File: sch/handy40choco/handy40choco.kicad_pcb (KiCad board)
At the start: 2 copper layers, 175 x 112 mm, 147 parts, among them J1 Conn_01x02, J2 Conn_02x08_Odd_Even, J3 USB_C_Receptacle_USB2.0_16P, J4 Conn_01x04, Q1 DMG2301L, SW1 SW_Push, SW10 SW_Push, SW11 SW_Push, SW12 SW_Push, SW13 SW_Push, SW14 SW_Push, SW15 SW_Push, SW16 SW_Push, SW17 SW_Push, SW18 SW_Push, SW19 SW_Push, SW2 SW_Push, SW20 SW_Push, SW21 SW_Push, SW22 SW_Push, SW23 SW_Push, SW24 SW_Push, SW25 SW_Push, SW26 SW_Push, SW27 SW_Push, SW28 SW_Push, SW29 SW_Push, SW3 SW_Push, SW30 SW_Push, SW31 SW_Push, SW32 SW_Push, SW33 SW_Push, SW34 SW_Push, SW35 SW_Push, SW36 SW_Push, SW37 SW_Push, SW38 SW_Push, SW39 SW_Push, SW4 SW_Push, SW40 SW_Push, SW41 SW_Push, SW42 SW_Push, SW5 SW_Push, SW6 SW_Push, SW7 SW_Push, SW8 SW_Push, SW9 SW_Push, U1 Pico, U2 pimoroni lcd, U3 ESP32-S3-WROOM-1, U4 MIC5219-3.3YM5, Y1 32k

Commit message: Kicad 9に変更しました。 マイコン基板から16ピンのピンヘッダに変更しました。
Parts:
- removed C1: 10u, Capacitor_SMD:C_0603_1608Metric_Pad1.08x0.95mm_HandSolder
- removed C2, C3: 100n, Capacitor_SMD:C_0603_1608Metric_Pad1.08x0.95mm_HandSolder
- removed C4: 1u, Capacitor_SMD:C_0603_1608Metric_Pad1.08x0.95mm_HandSolder
- removed C5: 470p, Capacitor_SMD:C_0603_1608Metric_Pad1.08x0.95mm_HandSolder
- removed C6: 10n, Capacitor_SMD:C_0603_1608Metric_Pad1.08x0.95mm_HandSolder
- removed C7, C8: 15p, Capacitor_SMD:C_0603_1608Metric_Pad1.08x0.95mm_HandSolder
- removed D41, D42, D43: D_Schottky, Diode_SMD:D_SOD-123
- removed D44, D45, D46: D_TVS, Diode_SMD:D_SOD-123
- removed D47, D48, D49, D50, D51, D52, D53: LED, LED_SMD:LED_0603_1608Metric_Pad1.05x0.95mm_HandSolder
- removed F1: Polyfuse_Small, Fuse:Fuse_Littelfuse-NANO2-451_453
- removed J2: Conn_02x08_Odd_Even, my_pico:oled_PinSocket_2x08_P2.54mm_Vertical
- removed J3: USB_C_Receptacle_USB2.0_16P, Connector_USB:USB_C_Receptacle_XKB_U262-16XN-4BVC11
- removed J4: Conn_01x04, Connector_JST:JST_XH_B4B-XH-A_1x04_P2.50mm_Vertical
- removed Q1: DMG2301L, Package_TO_SOT_SMD:SOT-23
- removed R1, R11, R12, R2, R8, R9: 0, Resistor_SMD:R_0603_1608Metric
- removed R10: [10M], Resistor_SMD:R_0603_1608Metric
- removed R13, R14, R15, R16, R17, R18, R19: 1k, Resistor_SMD:R_0603_1608Metric
- removed R3, R4, R7: 10k, Resistor_SMD:R_0603_1608Metric
- removed R5, R6: 5.1k, Resistor_SMD:R_0603_1608Metric
- removed SW41, SW42: SW_Push, Button_Switch_SMD:SW_Push_SPST_NO_Alps_SKRK
- removed U1: Pico, my_pico:pico_no_dbg_smd_th_p0.85
- removed U2: pimoroni lcd, my_pico:pimoroni_lcd_p0.85
- removed U3: ESP32-S3-WROOM-1, RF_Module:ESP32-S3-WROOM-1
- removed U4: MIC5219-3.3YM5, Package_TO_SOT_SMD:SOT-23-5
- removed Y1: 32k, Crystal:Crystal_SMD_2012-2Pin_2.0x1.2mm_HandSoldering
- J1: value Conn_01x02 -> Conn_01x20; footprint Connector_JST:JST_PH_B2B-PH-K_1x02_P2.00mm_Vertical -> Connector_PinHeader_2.54mm:PinHeader_1x20_P2.54mm_Vertical
- moved J1 35.9 mm to (210.0, 87.0), turned to -90 degrees
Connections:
- J1 pad 1: /VBAT -> /ROW3
- J1 pad 2: GND -> /ROW2
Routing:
- net +3.3V: track 170.8 -> 0.00 mm, vias 3 -> 0
- net /COL0: track 216.7 -> 61.8 mm
- net /COL1: track 206.4 -> 65.9 mm
- net /COL2: track 186.6 -> 57.9 mm
- net /COL3: track 173.0 -> 60.4 mm
- net /LCD_RESET: track 111.5 -> 0.00 mm
- net /COL4: track 155.4 -> 58.4 mm
- net /LCD_TE: track 92.0 -> 0.00 mm
- net /LCD_BL: track 86.7 -> 0.00 mm
- net /ROW3: track 291.0 -> 204.5 mm
- net /COL5: track 142.1 -> 60.4 mm
- net /COL6: track 132.1 -> 57.9 mm
- net /OLED_RESET: track 71.9 -> 0.00 mm
- net /ROW2: track 274.4 -> 205.2 mm
- net /DATA: track 61.2 -> 0.00 mm
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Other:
- board size 175 x 112 mm -> 175 x 72.5 mm

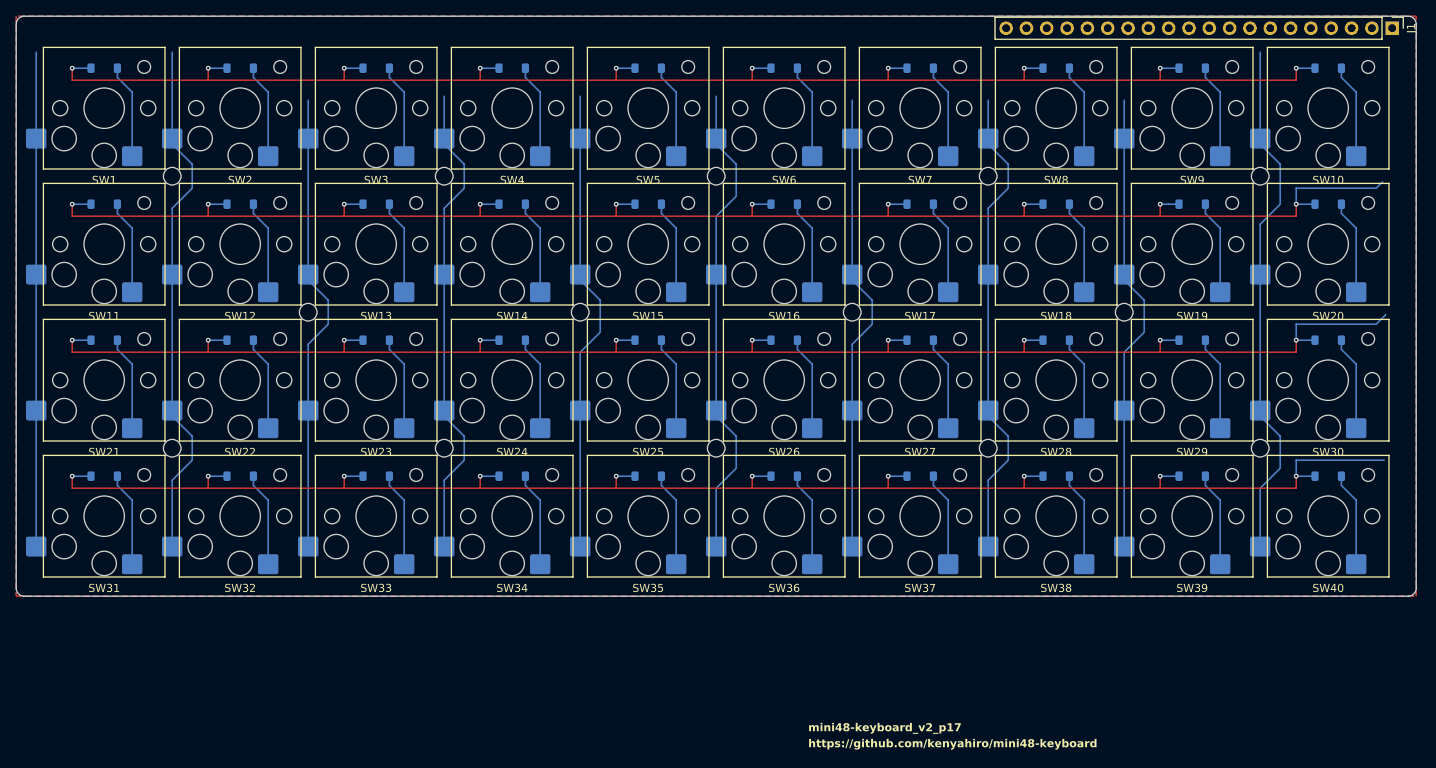
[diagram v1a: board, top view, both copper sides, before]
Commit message: 配線を完了しました。 シルクの位置を調整しました。
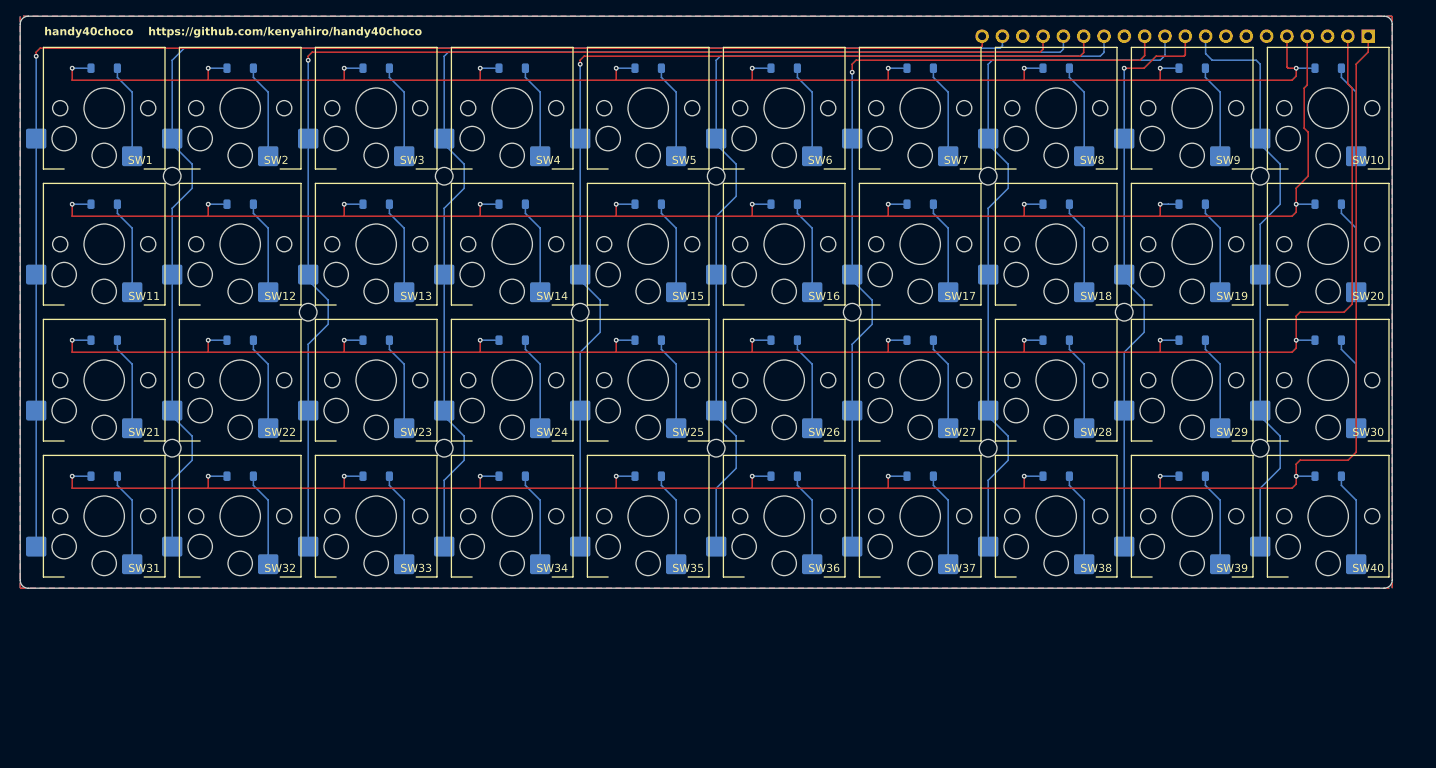
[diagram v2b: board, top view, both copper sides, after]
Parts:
- J1: moved to B.Cu
- SW1, SW10, SW11, SW12, SW13, SW14, SW15, SW16, SW17, SW18, SW19, SW2, SW20, SW21, SW22, SW23, SW24, SW25, SW26, SW27, SW28, SW29, SW3, SW30, SW31, SW32, SW33, SW34, SW35, SW36, SW37, SW38, SW39, SW4, SW40, SW5, SW6, SW7, SW8, SW9: footprint my_keyswitch:SW_Hotswap_Kailh_Choc_V1V2 -> my_keyswitch:SW_Hotswap_Kailh_Choc_V1V2_no_mp
- moved J1 3.16 mm to (207.0, 88.0), turned to 90 degrees
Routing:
- net /COL0: track 61.8 -> 181.6 mm, vias 0 -> 1
- net /COL1: track 65.9 -> 170.7 mm
- net /COL2: track 57.9 -> 157.2 mm, vias 0 -> 1
- net /COL3: track 60.4 -> 144.8 mm
- net /COL4: track 58.4 -> 128.3 mm, vias 0 -> 1
- net /COL5: track 60.4 -> 115.8 mm
- net /ROW3: track 204.5 -> 253.4 mm
- net /COL6: track 57.9 -> 101.8 mm, vias 0 -> 1
- net /ROW2: track 205.2 -> 235.6 mm
- net /COL7: track 59.9 -> 89.4 mm
- net /COL8: track 57.9 -> 72.6 mm, vias 0 -> 1
- net /ROW1: track 204.6 -> 213.2 mm
- net /COL9: track 65.9 -> 74.0 mm
- net /ROW0: track 191.5 -> 196.3 mm
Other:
- board size 175 x 72.5 mm -> 171.5 x 71.5 mm
- board text added: "handy40choco"
- board text added: "https://github.com/kenyahiro/handy40choco"
- board text removed: "https://github.com/kenyahiro/mini48-keyboard"
- board text removed: "mini48-keyboard_v2_p17"

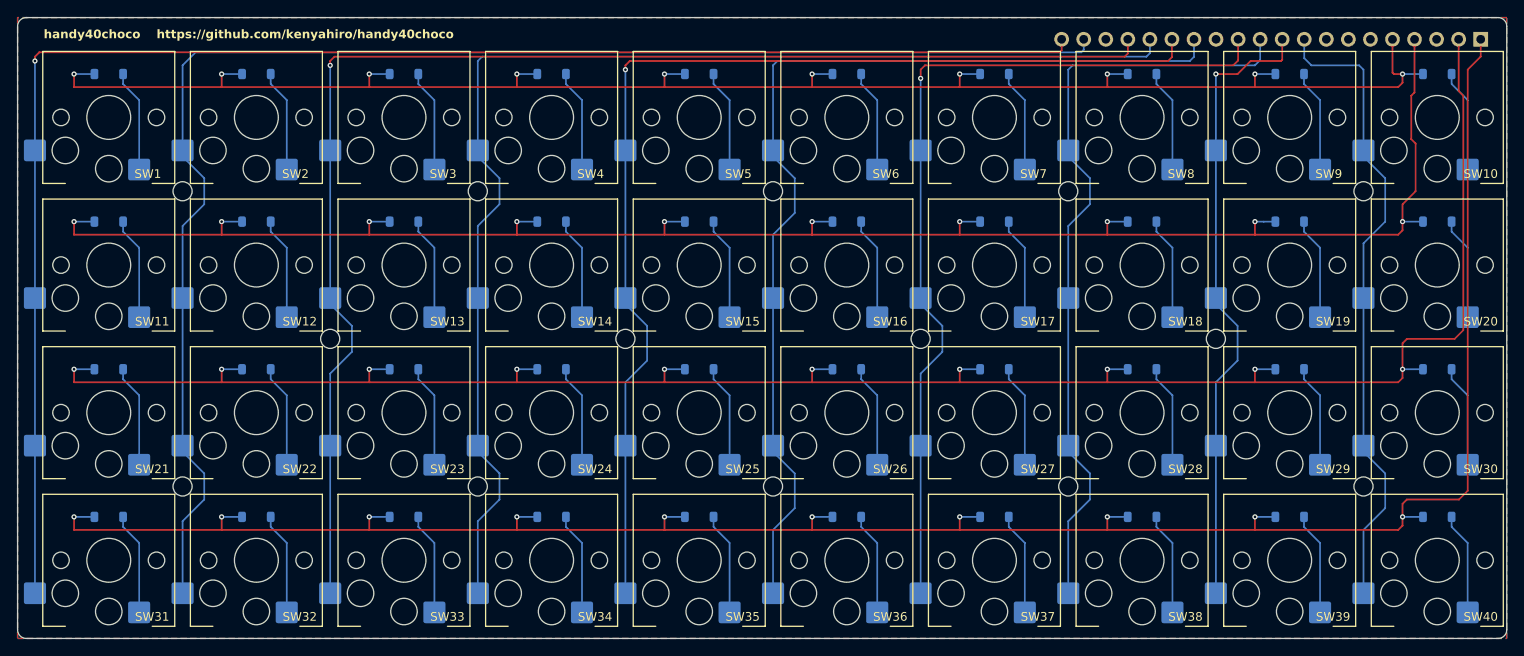
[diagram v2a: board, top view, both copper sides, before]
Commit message: 電気図面のpdfを追加しました。 PCBのFABにピンヘッダの寸法線を追記しました。
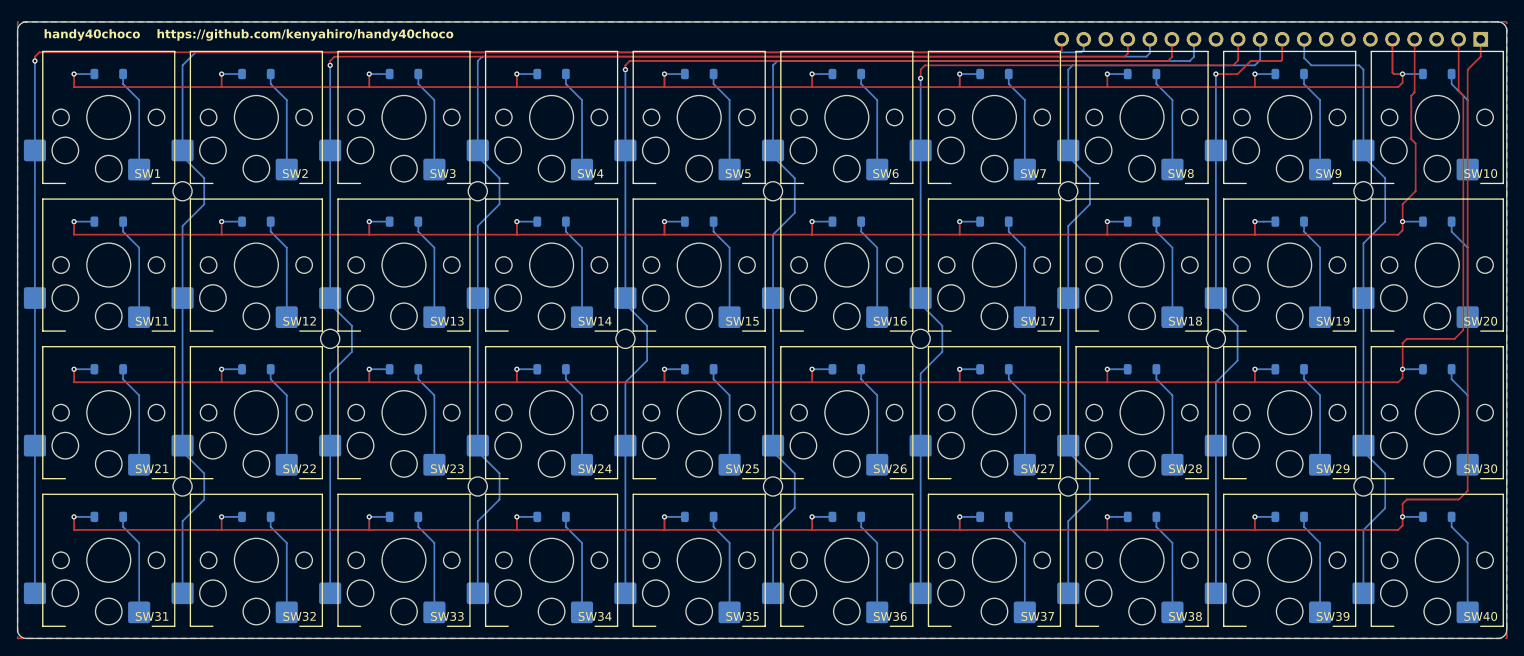
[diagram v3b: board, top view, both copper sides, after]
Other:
- board size 171.5 x 71.5 mm -> 171.5 x 71 mm
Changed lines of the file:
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@@
 		(allow_soldermask_bridges_in_footprints no)
 		(tenting front back)
-		(aux_axis_origin 38.5 85.5)
-		(grid_origin 38.5 85.5)
+		(aux_axis_origin 38.5 86)
+		(grid_origin 38.5 86)
 		(pcbplotparams
-			(layerselection 0x00000000_00000000_55555555_5755f5ff)
-			(plot_on_all_layers_selection 0x00000000_00000000_00000000_00000000)
+			(layerselection 0x00000000_00000000_5555555d_5755f5ff)
+			(plot_on_all_layers_selection 0x00000000_00000000_00000008_00000000)
 			(disableapertmacros no)
 			(usegerberextensions yes)
@@
 			(dashed_line_gap_ratio 3.000000)
 			(svgprecision 4)
-			(plotframeref no)
+			(plotframeref yes)
 			(mode 1)
 			(useauxorigin no)
@@
 			(pdf_back_fp_property_popups yes)
 			(pdf_metadata yes)
-			(pdf_single_document no)
+			(pdf_single_document yes)
 			(dxfpolygonmode yes)
 			(dxfimperialunits yes)
@@
 			(psnegative no)
 			(psa4output no)
-			(plot_black_and_white yes)
+			(plot_black_and_white no)
 			(sketchpadsonfab no)
 			(plotpadnumbers no)
@@
 			(crossoutdnponfab yes)
 			(subtractmaskfromsilk yes)
-			(outputformat 1)
+			(outputformat 4)
 			(mirror no)
-			(drillshape 0)
+			(drillshape 2)
 			(scaleselection 1)
 			(outputdirectory "gerber")
@@
 	)
 	(gr_arc
-		(start 209 85.5)
-		(mid 209.707107 85.792893)
-		(end 210 86.5)
+		(start 209 86)
+		(mid 209.707107 86.292893)
+		(end 210 87)
 		(stroke
 			(width 0.05)
@@
 	)
 	(gr_line
-		(start 210 86.5)
+		(start 210 87)
 		(end 210 156)
 		(stroke
@@
 	)
 	(gr_line
-		(start 39.5 85.5)
-		(end 209 85.5)
+		(start 39.5 86)
+		(end 209 86)
 		(stroke
 			(width 0.05)
@@
 	(gr_line
 		(start 38.5 156)
-		(end 38.5 86.5)
+		(end 38.5 87)
 		(stroke
 			(width 0.05)
@@
 	)
 	(gr_arc
-		(start 38.5 86.5)
-		(mid 38.792893 85.792893)
-		(end 39.5 85.5)
+		(start 38.5 87)
+		(mid 38.792893 86.292893)
+		(end 39.5 86)
 		(stroke
 			(width 0.05)
@@
 		(layer "F.Fab")
 		(pts
-			(xy 210 85.5) (xy 210 157)
+			(xy 209 86) (xy 209 157)
 		)
-		(height 53)
+		(height 55.5)
 		(orientation 1)
 		(format
@@
 			(keep_text_aligned yes)
 		)
-		(gr_text "71.5000 mm"
-			(at 261.85 121.25 90)
+		(gr_text "71.0000 mm"
+			(at 263.35 121.5 90)
+			(layer "F.Fab")
+			(effects
+				(font
+					(size 1 1)
+					(thickness 0.15)
+				)
+			)
+		)
+	)
+	(dimension
+		(type orthogonal)
+		(layer "F.Fab")
+		(pts
+			(xy 207 88) (xy 210 88)
+		)
+		(height -15.5)
+		(orientation 0)
+		(format
+			(prefix "")
+			(suffix "")
+			(units 3)
+			(units_format 1)
+			(precision 4)
+		)
+		(style
+			(thickness 0.1)
+			(arrow_length 1.27)
+			(text_position_mode 0)
+			(arrow_direction outward)
+			(extension_height 0.58642)
+			(extension_offset 0.5)
+			(keep_text_aligned yes)
+		)
+		(gr_text "3.0000 mm"
+			(at 208.5 71.35 0)
+			(layer "F.Fab")
+			(effects
+				(font
+					(size 1 1)
+					(thickness 0.15)
+				)
+			)
+		)
+	)
+	(dimension
+		(type orthogonal)
+		(layer "F.Fab")
+		(pts
+			(xy 207 88) (xy 207 86)
+		)
+		(height 17)
+		(orientation 1)
+		(format
+			(prefix "")
+			(suffix "")
+			(units 3)
+			(units_format 1)
+			(precision 4)
+		)
+		(style
+			(thickness 0.1)
+			(arrow_length 1.27)
+			(text_position_mode 0)
+			(arrow_direction outward)
+			(extension_height 0.58642)
+			(extension_offset 0.5)
+			(keep_text_aligned yes)
+		)
+		(gr_text "2.0000 mm"
+			(at 222.85 87 90)
 			(layer "F.Fab")
 			(effects
@@
 		(polygon
 			(pts
-				(xy 38.5 85.5) (xy 38.5 157) (xy 210 157) (xy 210 85.5)
+				(xy 38.5 86) (xy 38.5 157) (xy 210 157) (xy 210 86)
 			)
 		)
@@
 		(polygon
 			(pts
-				(xy 38.5 85.5) (xy 38.5 157) (xy 210 157) (xy 210 85.5)
+				(xy 38.5 86) (xy 38.5 157) (xy 210 157) (xy 210 86)
 			)
 		)

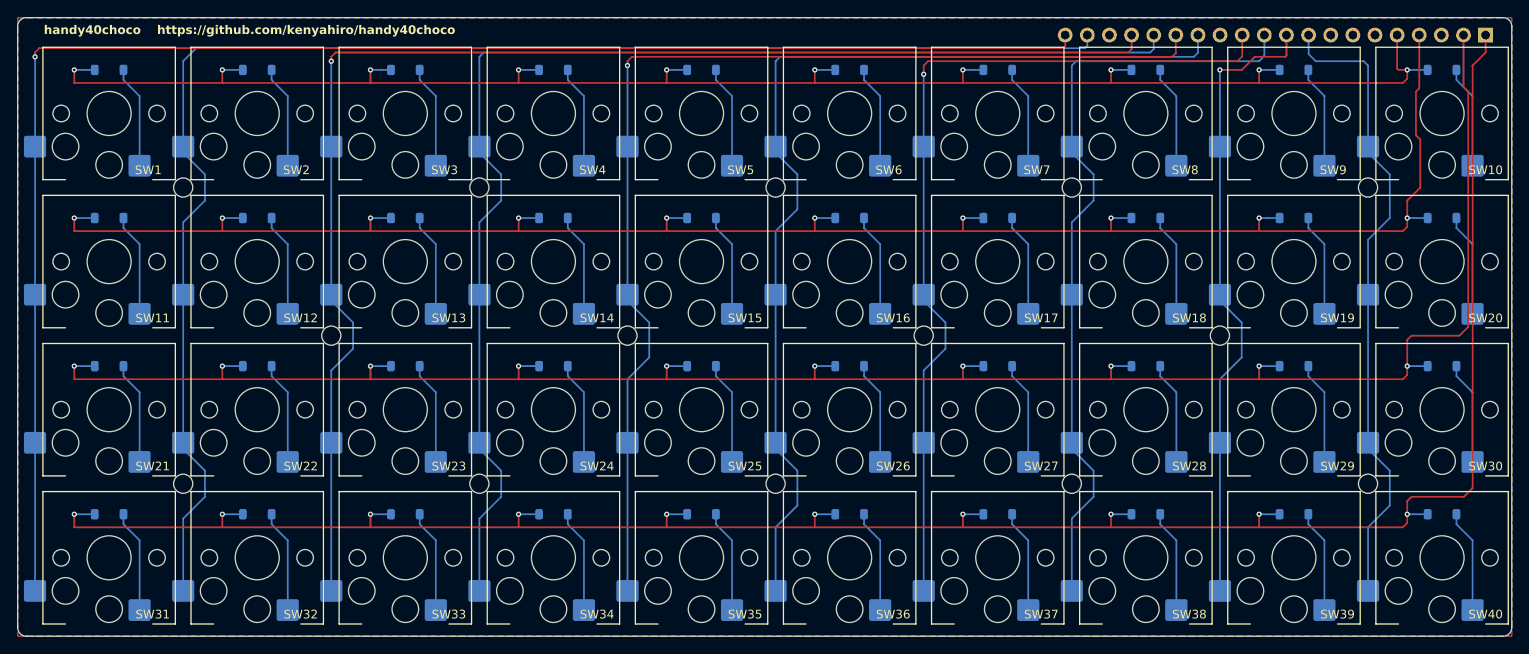
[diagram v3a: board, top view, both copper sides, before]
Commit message: 左端のキーの向きを180度回転させて、基板幅を短くしました。
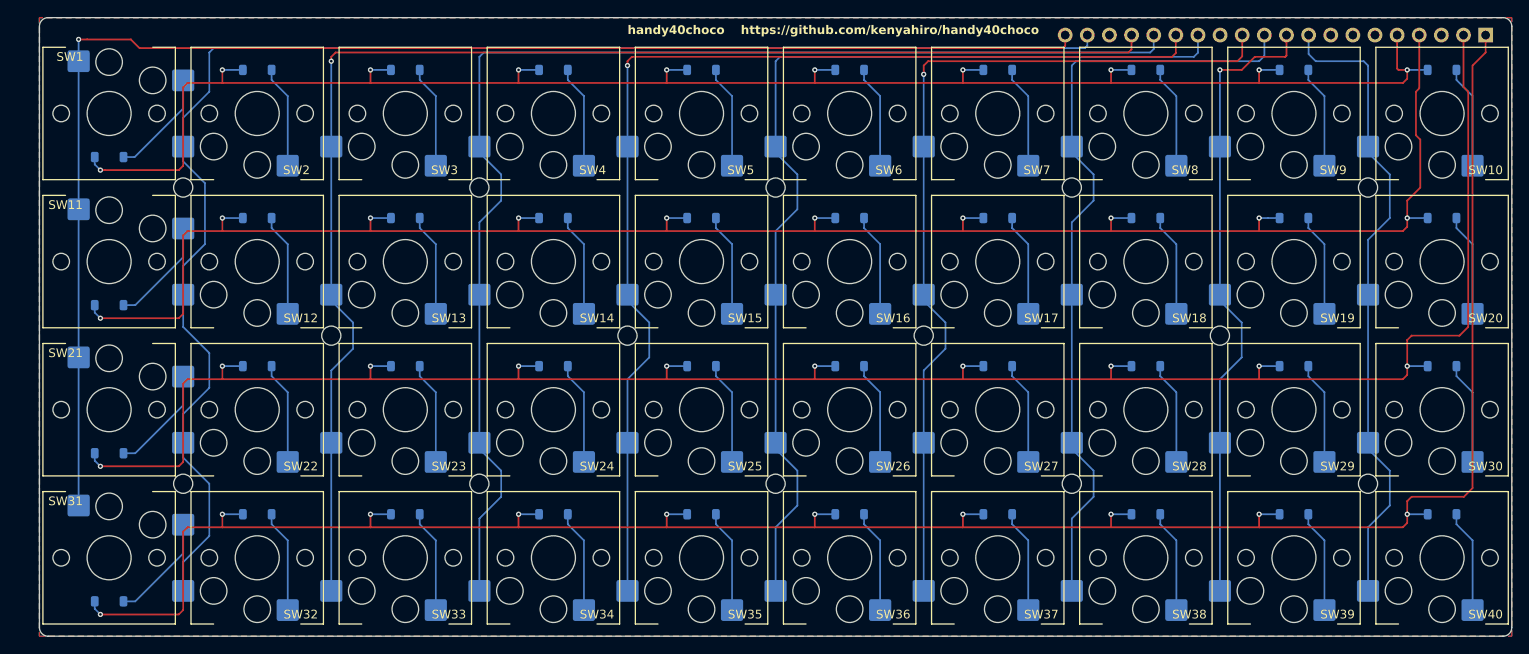
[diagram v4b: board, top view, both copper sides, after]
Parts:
- moved D1 10.0 mm to (49.0, 102.0)
- moved D11 10.0 mm to (49.0, 119.0)
- moved D21 10.0 mm to (49.0, 136.0)
- moved D31 10.0 mm to (49.0, 153.0)
- turned SW1 to 0 degrees
- turned SW11 to 0 degrees
- turned SW21 to 0 degrees
- turned SW31 to 0 degrees
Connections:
- SW1 pad 1: Net-(D1-A) -> /COL0
- SW1 pad 2: /COL0 -> Net-(D1-A)
- SW11 pad 1: Net-(D11-A) -> /COL0
- SW11 pad 2: /COL0 -> Net-(D11-A)
- SW21 pad 1: Net-(D21-A) -> /COL0
- SW21 pad 2: /COL0 -> Net-(D21-A)
- SW31 pad 1: Net-(D31-A) -> /COL0
- SW31 pad 2: /COL0 -> Net-(D31-A)
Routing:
- net /COL0: track 181.6 -> 168.5 mm
- net /ROW0: track 196.3 -> 200.8 mm
- net /ROW3: track 253.4 -> 257.8 mm
- net /ROW2: track 235.6 -> 239.9 mm
- net /ROW1: track 213.2 -> 217.5 mm
- net /COL1: track 170.7 -> 172.4 mm
- net Net-(D31-A): track 11.8 -> 12.4 mm
- net Net-(D21-A): track 11.8 -> 12.4 mm
- net Net-(D11-A): track 11.8 -> 12.4 mm
- net Net-(D1-A): track 11.8 -> 12.4 mm
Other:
- board size 171.5 x 71 mm -> 169 x 71 mm
